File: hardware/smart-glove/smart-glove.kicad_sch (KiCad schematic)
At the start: 6 parts

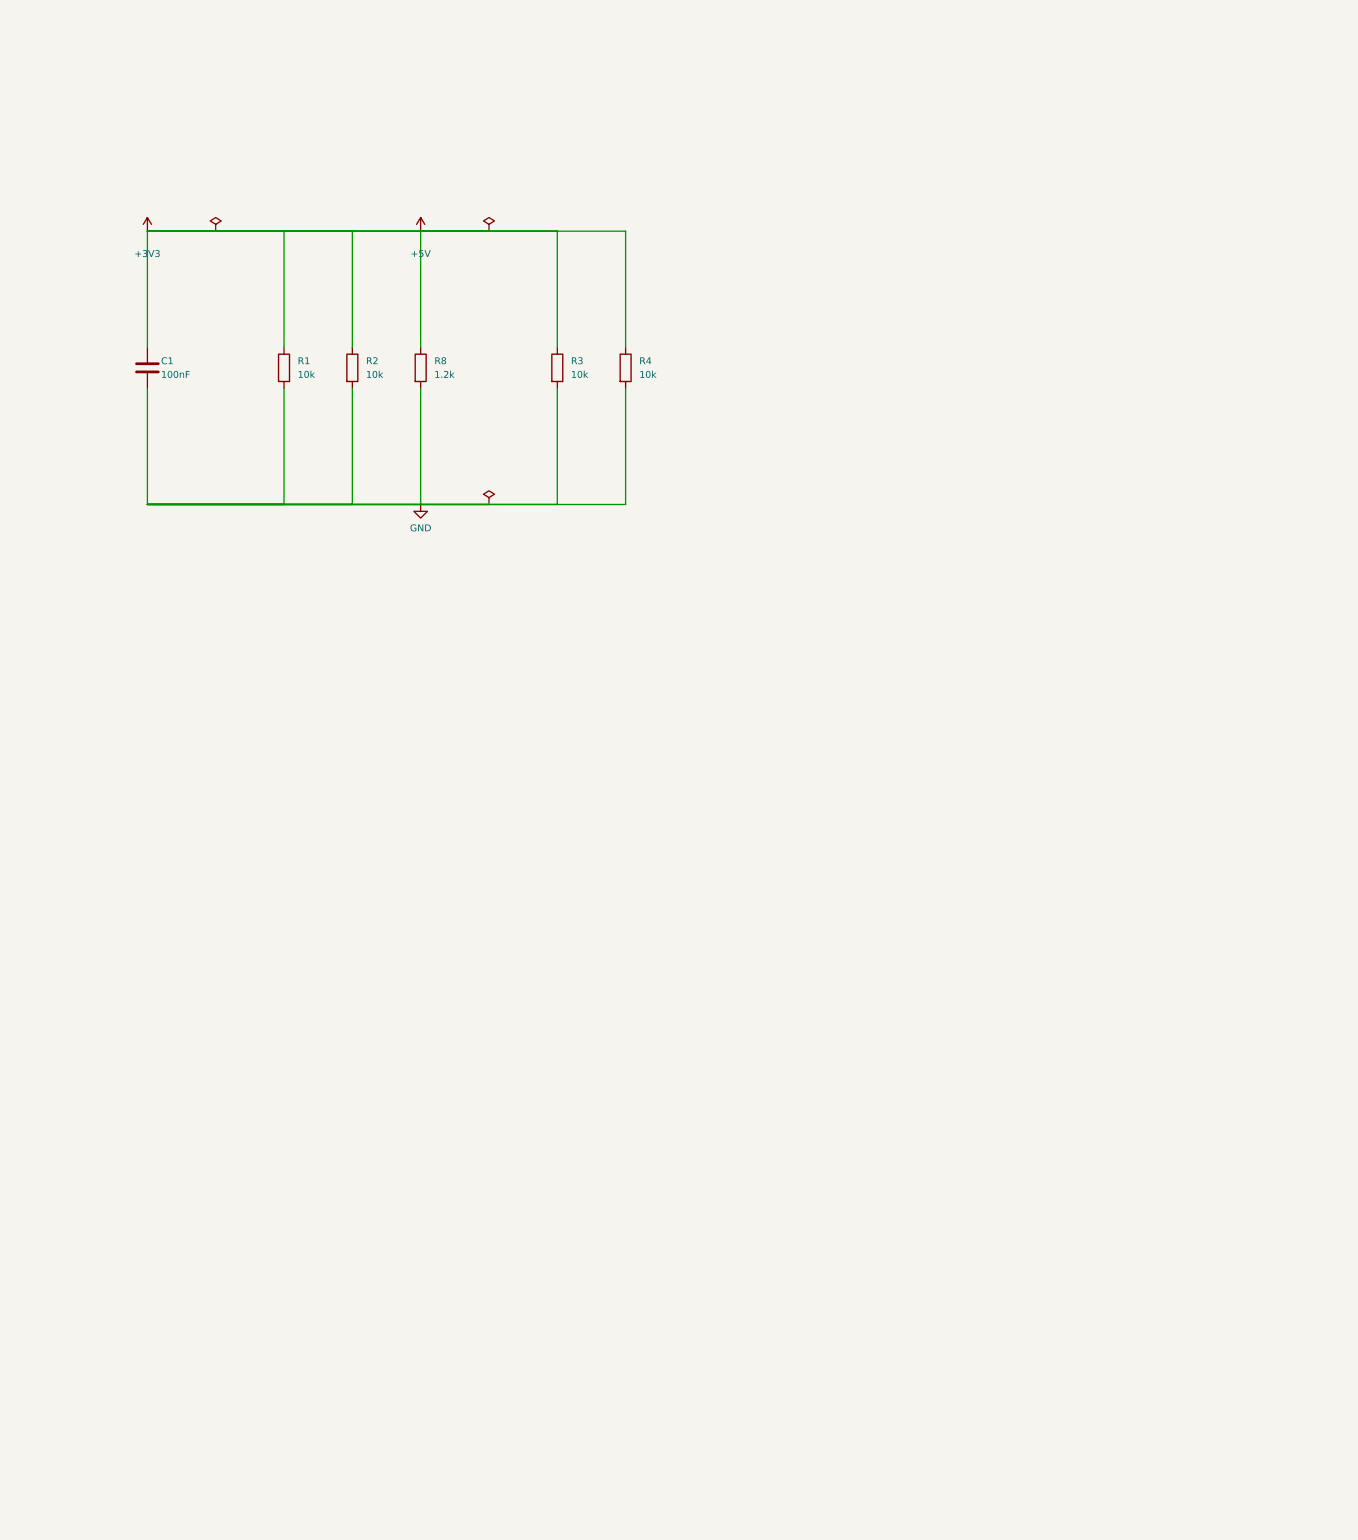
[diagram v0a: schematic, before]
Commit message: Complete Smart Glove KiCad schematic with ERC-clean nets
Add build_complete_schematic.py covering USB-C, TP4056, AMS1117,
ESP32, MPU-6050, flex dividers, LEDs/switches, and power flags.
Align PCB netlist (SCL on U1.36, REGOUT+C10, USB SBU NC) with schematic.

Co-authored-by: ADIL ZAHOOR  <adilzahoor2812@users.noreply.github.com>
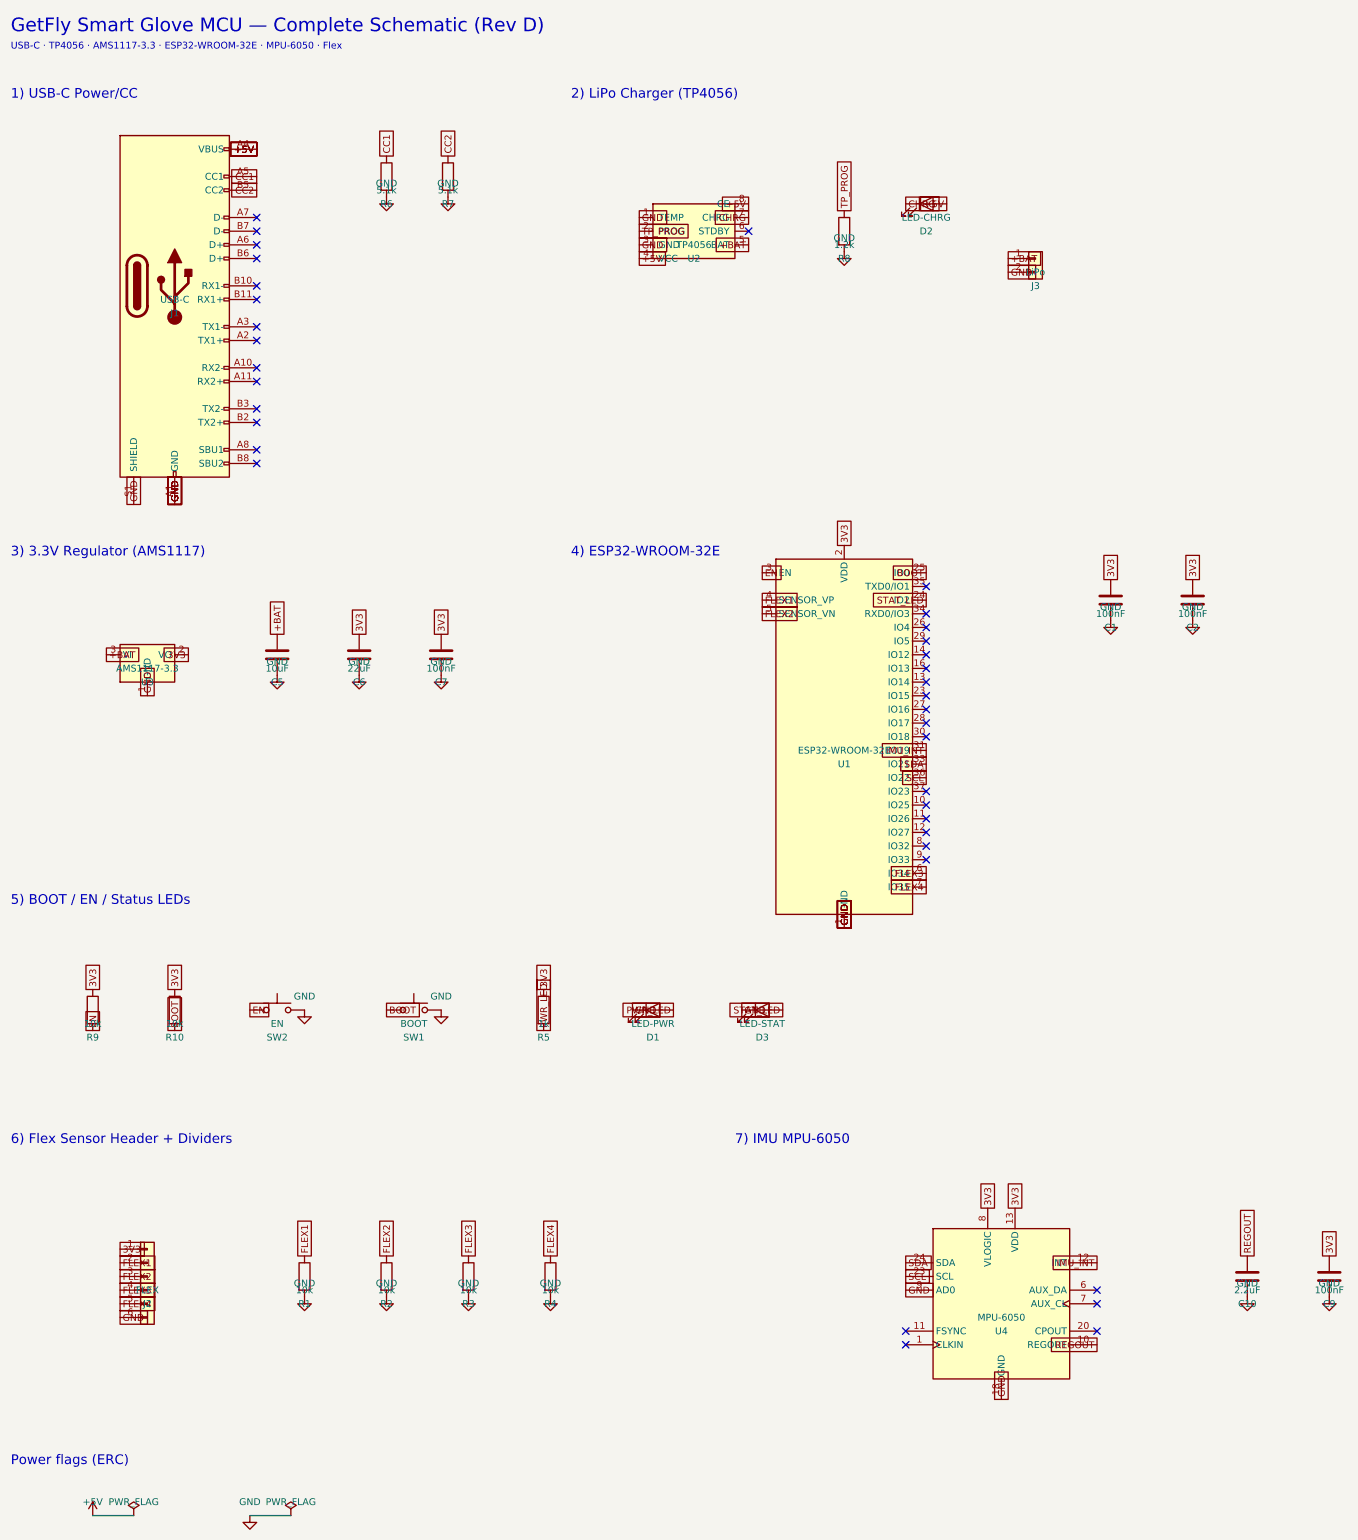
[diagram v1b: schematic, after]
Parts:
- added C10: 2.2uF, Capacitor_SMD:C_0603_1608Metric, symbol Device:C
- added C2, C7, C9: 100nF, Capacitor_SMD:C_0603_1608Metric, symbol Device:C
- added C5: 10uF, Capacitor_SMD:C_0805_2012Metric, symbol Device:C
- added C6: 22uF, Capacitor_SMD:C_0805_2012Metric, symbol Device:C
- added D1: LED-PWR, LED_SMD:LED_0603_1608Metric, symbol Device:LED
- added D2: LED-CHRG, LED_SMD:LED_0603_1608Metric, symbol Device:LED
- added D3: LED-STAT, LED_SMD:LED_0603_1608Metric, symbol Device:LED
- added J1: USB-C, Connector_USB:USB_C_Receptacle_HRO_TYPE-C-31-M-12, symbol Connector:USB_C_Receptacle
- added J2: FLEX, Connector_PinHeader_2.54mm:PinHeader_1x06_P2.54mm_Vertical, symbol Connector_Generic:Conn_01x06
- added J3: LiPo, Connector_JST:JST_PH_B2B-PH-K_1x02_P2.00mm_Vertical, symbol Connector_Generic:Conn_01x02
- added R10, R9: 10k, Resistor_SMD:R_0603_1608Metric, symbol Device:R
- added R5: 1k, Resistor_SMD:R_0603_1608Metric, symbol Device:R
- added R6, R7: 5.1k, Resistor_SMD:R_0603_1608Metric, symbol Device:R
- added SW1: BOOT, Button_Switch_SMD:SW_SPST_B3U-1000P, symbol Switch:SW_Push
- added SW2: EN, Button_Switch_SMD:SW_SPST_B3U-1000P, symbol Switch:SW_Push
- added U1: ESP32-WROOM-32E, RF_Module:ESP32-WROOM-32, symbol RF_Module:ESP32-WROOM-32E
- added U2: TP4056, Package_SO:SOIC-8_3.9x4.9mm_P1.27mm, symbol Device:TP4056
- added U3: AMS1117-3.3, Package_TO_SOT_SMD:SOT-223, symbol Device:AMS1117-3.3
- added U4: MPU-6050, Sensor_Motion:InvenSense_QFN-24_4x4mm_P0.5mm, symbol Sensor_Motion:MPU-6050
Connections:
- net GND: now also C10.2, C2.2, C5.2, C6.2, C7.2, C9.2, D1.1 (K), D3.1 (K), J1.A1 (GND), J1.A12 (GND), J1.B1 (GND), J1.B12 (GND), J1.S1 (SHIELD), J2.6 (Pin_6), J3.2 (Pin_2), R6.2, R7.2, SW1.2, SW2.2, U1.1 (GND), U1.15 (GND), U1.38 (GND), U1.39 (GND), U2.1 (TEMP), U2.3 (GND), U3.1 (GND), U4.18 (GND), U4.9 (AD0)
- removed net +3V3: C1.1, R1.1, R2.1, R3.1, R4.1, R8.1
- new net +5V: D2.2 (A), J1.A4 (VBUS), J1.A9 (VBUS), J1.B4 (VBUS), J1.B9 (VBUS), U2.4 (VCC), U2.8 (CE)
- new net +BAT: C5.1, J3.1 (Pin_1), U2.5 (BAT), U3.3 (VI)
- new net 3V3: C1.1, C2.1, C6.1, C7.1, C9.1, J2.1 (Pin_1), R10.1, R5.1, R9.1, U1.2 (VDD), U3.2 (VO), U4.13 (VDD), U4.8 (VLOGIC)
- new net BOOT: R10.2, SW1.1, U1.25 (IO0)
- new net CC1: J1.A5 (CC1), R6.1
- new net CC2: J1.B5 (CC2), R7.1
- new net CHRG: D2.1 (K), U2.7 (CHRG)
- new net EN: R9.2, SW2.1, U1.3 (EN)
- new net FLEX1: J2.2 (Pin_2), R1.1, U1.4 (SENSOR_VP)
- new net FLEX2: J2.3 (Pin_3), R2.1, U1.5 (SENSOR_VN)
- new net FLEX3: J2.4 (Pin_4), R3.1, U1.6 (IO34)
- new net FLEX4: J2.5 (Pin_5), R4.1, U1.7 (IO35)
- new net IMU_INT: U1.31 (IO19), U4.12 (INT)
- new net PWR_LED: D1.2 (A), R5.2
- new net REGOUT: C10.1, U4.10 (REGOUT)
- new net SCL: U1.36 (IO22), U4.23 (SCL)
- new net SDA: U1.33 (IO21), U4.24 (SDA)
- new net STAT_LED: D3.2 (A), U1.24 (IO2)
- new net TP_PROG: R8.1, U2.2 (PROG)
- no-connect marks 0 -> 37
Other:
- note added: "1) USB-C Power/CC"
- note added: "2) LiPo Charger (TP4056)"
- note added: "3) 3.3V Regulator (AMS1117)"
- note added: "4) ESP32-WROOM-32E"
- note added: "5) BOOT / EN / Status LEDs"
- note added: "6) Flex Sensor Header + Dividers"
- note added: "7) IMU MPU-6050"
- note added: "GetFly Smart Glove MCU — Complete Schematic (Rev D)"
- note added: "Power flags (ERC)"
- note added: "USB-C · TP4056 · AMS1117-3.3 · ESP32-WROOM-32E · MPU-6050 · Flex"
- title: Smart Glove MCU -> GetFly Smart Glove MCU
